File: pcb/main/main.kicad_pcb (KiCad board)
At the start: 2 copper layers, 50 parts, among them J1 Conn_01x08, J2 Conn_ARM_JTAG_SWD_10, J3 Conn_01x08, J4 USB4085-GF-A, J5 Conn_02x02_Odd_Even, J6 Conn_02x02_Odd_Even, J7 Conn_02x02_Odd_Even, SW1 SW_Push, SW2 Rotary_Encoder_Switch, SW3 Rotary_Encoder_Switch, U1 ATSAMD21E18A-AF, U2 LP3990MF-3.3_NOPB

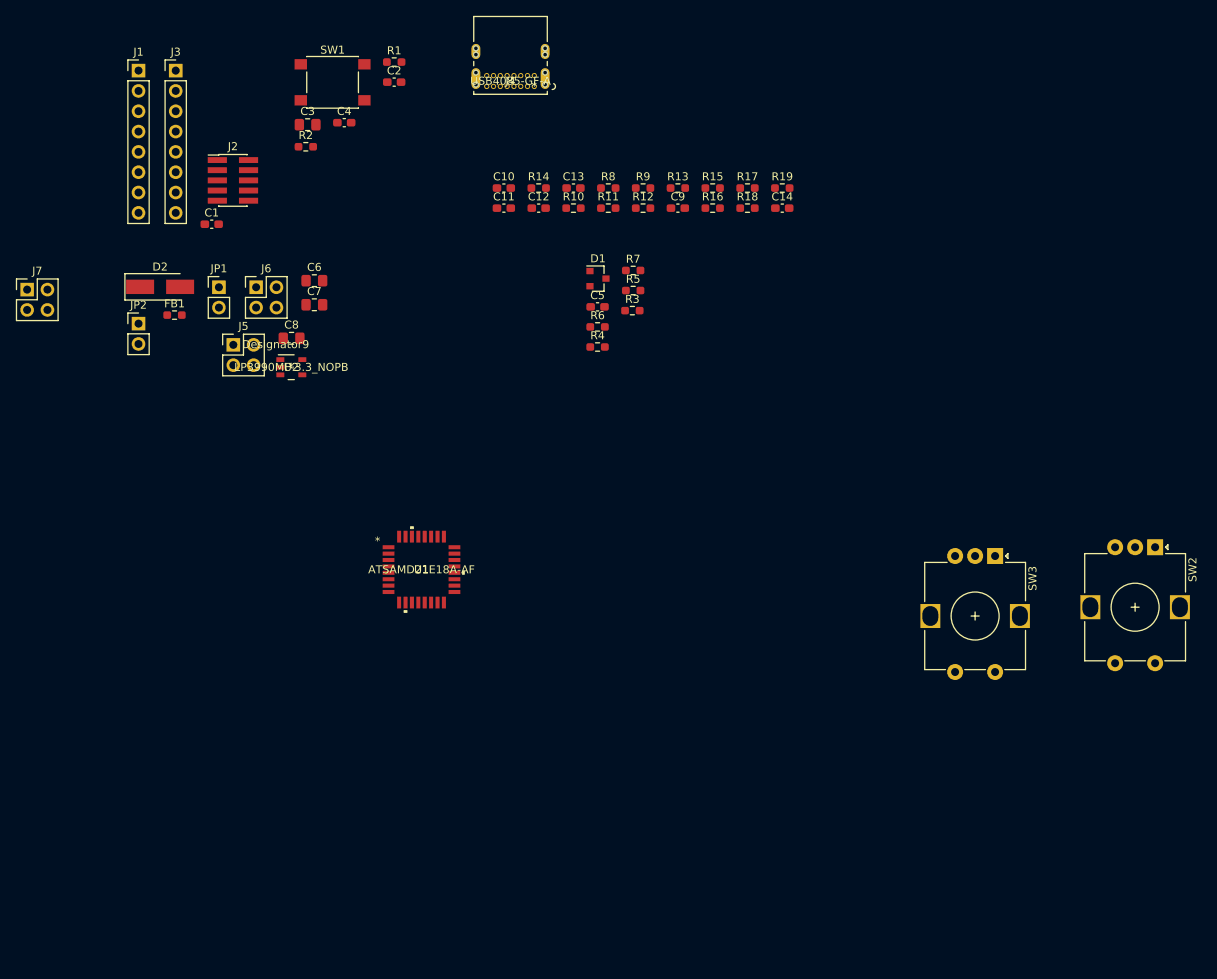
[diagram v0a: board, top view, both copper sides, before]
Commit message: Finished PCB layout
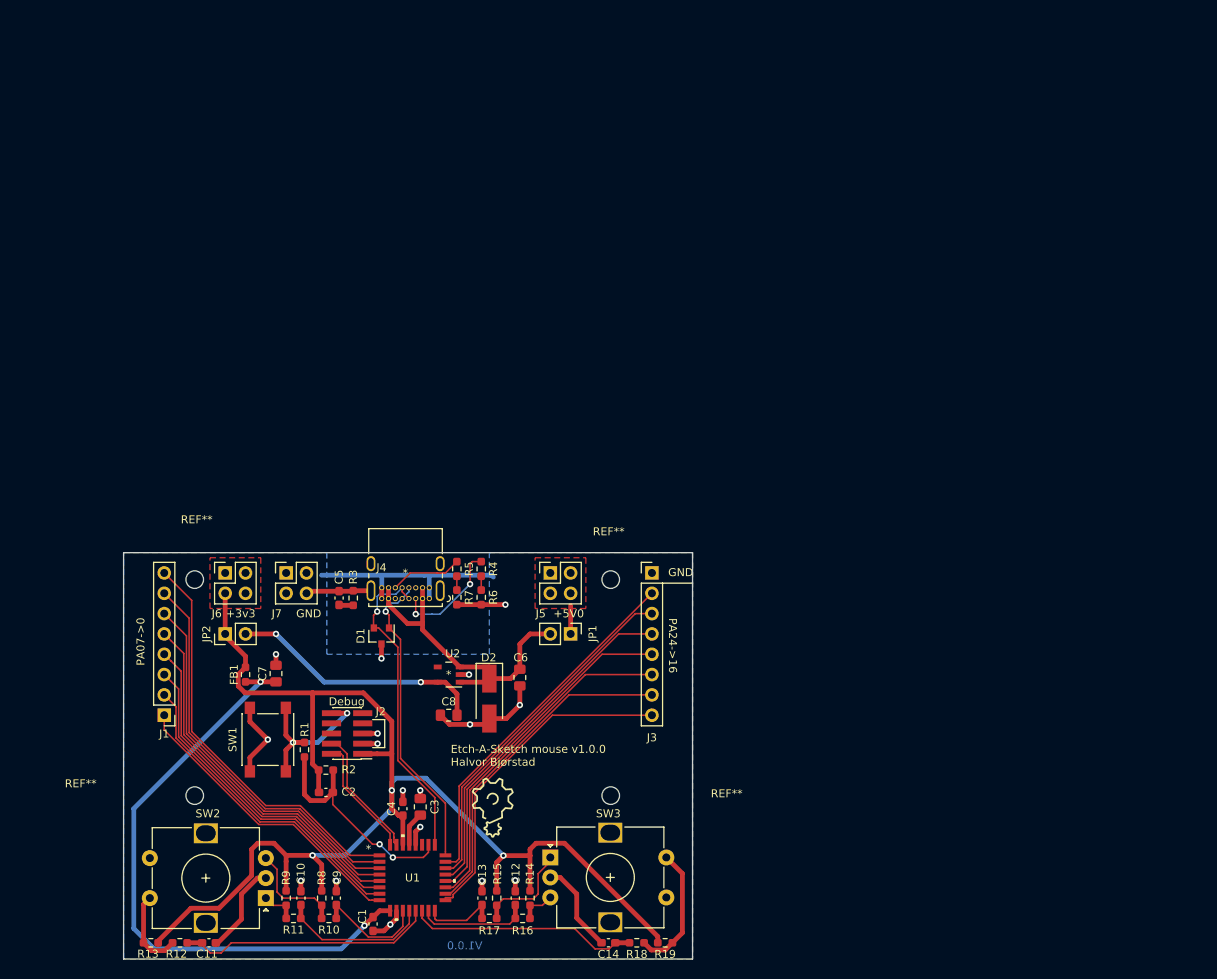
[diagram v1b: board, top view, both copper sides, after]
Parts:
- added G***: LOGO, footprints:icon, F.Cu at (132.5, 151.2)
- added REF**: MountingHole_2.2mm_M2, MountingHole:MountingHole_2.2mm_M2, F.Cu at (147.2, 149.8)
- added REF**: MountingHole_2.2mm_M2, MountingHole:MountingHole_2.2mm_M2, F.Cu at (95.2, 149.8)
- added REF**: MountingHole_2.2mm_M2, MountingHole:MountingHole_2.2mm_M2, F.Cu at (95.2, 122.8)
- added REF**: MountingHole_2.2mm_M2, MountingHole:MountingHole_2.2mm_M2, F.Cu at (147.2, 122.8)
- moved SW2 119.5 mm to (104.1, 162.6), turned to 180 degrees
- moved R13 115.1 mm to (89.8, 168.1), turned to 180 degrees
- moved R12 108.6 mm to (93.4, 168.1)
- moved R9 99.3 mm to (106.7, 162.6), turned to 90 degrees
- moved C11 99.0 mm to (97.0, 168.1)
- moved R11 97.1 mm to (107.6, 165.1), turned to 180 degrees
- moved R17 96.8 mm to (132.1, 165.1)
- moved C9 96.2 mm to (113.0, 162.6), turned to 90 degrees
- moved R8 95.7 mm to (111.1, 162.6), turned to 90 degrees
- moved R19 95.5 mm to (154.1, 168.1)
- moved C14 94.4 mm to (147.0, 168.1), turned to 180 degrees
- moved R10 93.9 mm to (112.0, 165.1), turned to 180 degrees
- moved R18 92.9 mm to (150.5, 168.1), turned to 180 degrees
- moved R15 92.8 mm to (133.0, 162.6), turned to 90 degrees
- moved C10 92.3 mm to (108.5, 162.6), turned to 90 degrees
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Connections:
- J3 pad 1: Net-(J3-Pad1) -> GND
- J4 pad 17: GND -> Net-(J4-Pad17)
- J4 pad 19: GND -> Net-(J4-Pad19)
- J4 pad 20: GND -> Net-(J4-Pad20)
- JP2 pad 1: Net-(C8-Pad1) -> +3V3
- JP2 pad 2: +3V3 -> Net-(C8-Pad1)
- U1 pad 11: /UI.sch/RC_Left_A -> /UI.sch/RC_Left_B
- U1 pad 12: /UI.sch/RC_Left_B -> /UI.sch/RC_Left_A
- U1 pad 14: /UI.sch/RC_Right_A -> /UI.sch/SW_Right
- U1 pad 16: /UI.sch/SW_Right -> /UI.sch/RC_Right_A
- U1 pad 27: Net-(J3-Pad1) -> Net-(U1-Pad27)
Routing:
- net +3V3: track 0.00 -> 172.4 mm, vias 0 -> 3
- net GND: track 0.00 -> 111.6 mm, vias 0 -> 17
- net +3.3VA: track 0.00 -> 76.3 mm, vias 0 -> 2
- net Net-(J1-Pad8): track 0.00 -> 51.1 mm
- net Net-(J1-Pad7): track 0.00 -> 49.2 mm
- net Net-(J1-Pad6): track 0.00 -> 47.3 mm
- net Net-(J1-Pad5): track 0.00 -> 45.3 mm
- net Net-(J3-Pad2): track 0.00 -> 45.0 mm
- net Net-(J3-Pad3): track 0.00 -> 44.3 mm
- net Net-(J3-Pad4): track 0.00 -> 43.8 mm
- net Net-(J1-Pad4): track 0.00 -> 43.4 mm
- net Net-(J3-Pad5): track 0.00 -> 43.2 mm
- net Net-(J3-Pad6): track 0.00 -> 42.7 mm
- net Net-(J3-Pad7): track 0.00 -> 42.0 mm
- net Net-(J3-Pad8): track 0.00 -> 41.6 mm
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- added copper zone on F.Cu, net +3V3
- added copper zone on F.Cu, net +5V
- added copper zone on B.Cu, net GND
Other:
- board outline added: 71.1 x 50.8 mm
- net class Default: clearance 0.2 -> 0.127; trace_width 0.25 -> 0.2
- rule trace_clearance: 0.2 -> 0.127
- board text added: "+3v3"
- board text added: "+5V0"
- board text added: "Debug"
- board text added: "Etch-A-Sketch mouse v1.0.0 Halvor Bjørstad"
- board text added: "GND"
- board text added: "PA07->0"
- board text added: "PA24->16"
- board text added: "V1.0.0"
